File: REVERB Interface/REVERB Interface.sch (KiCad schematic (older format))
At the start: 17 parts, among them J1 RPiZeroW, J2 Iridium, J3 APRS, J4 Antenna, J5 MAX3232BOB, J5 USB, J6 USBSER2, J7 USBSER3, J8 USBSER1, U1 AT25P, U2 MAX3232

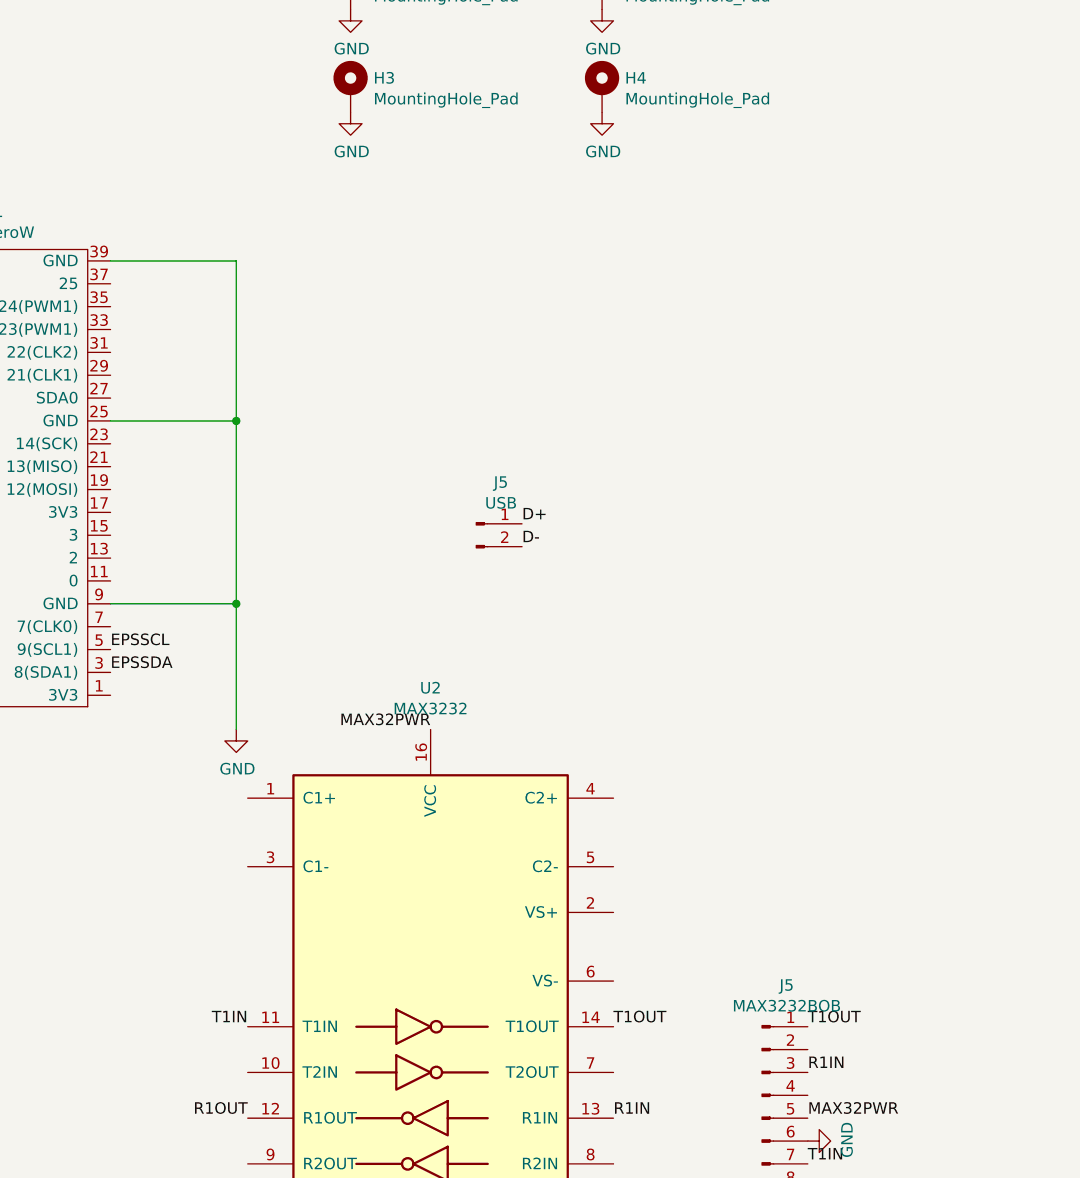
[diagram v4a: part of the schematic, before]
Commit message: add capacitors to max3232
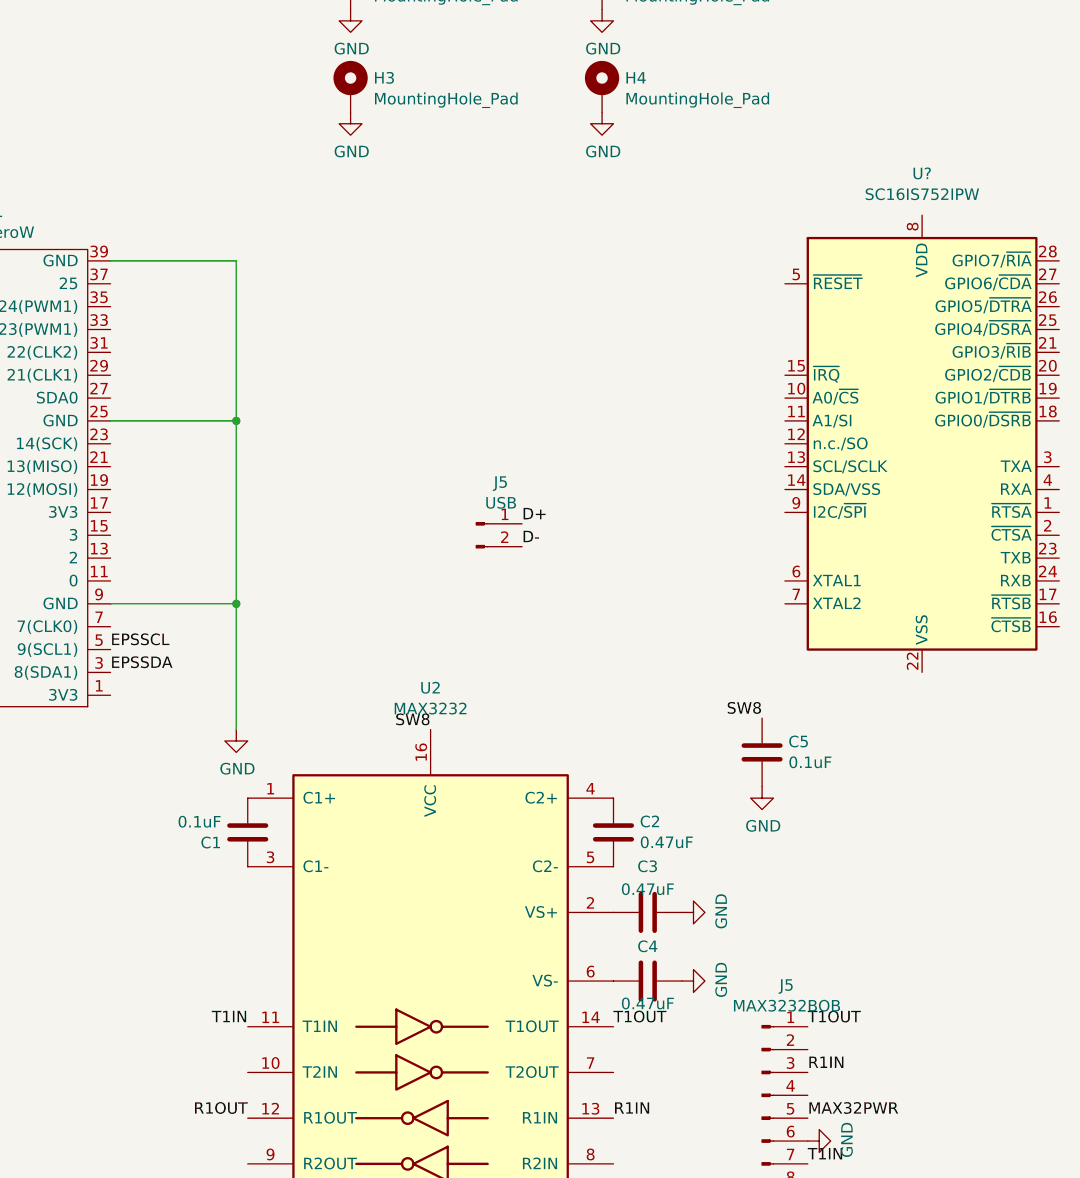
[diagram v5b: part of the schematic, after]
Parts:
- added C1, C5: 0.1uF, symbol Device:C
- added C2, C3, C4: 0.47uF, symbol Device:C
- added U?: SC16IS752IPW, Package_SO:TSSOP-28_4.4x9.7mm_P0.65mm, symbol Interface_UART:SC16IS752IPW
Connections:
- net GND: now also C3.1, C4.1, C5.2
- net MAX32PWR: no longer U2.16 (VCC)
- net SW8: now also U2.16 (VCC), C5.1
- net at U2.1 (C1+): now also C1.2
- net at U2.2 (VS+): now also C3.2
- net at U2.3 (C1-): now also C1.1
- net at U2.4 (C2+): now also C2.1
- net at U2.5 (C2-): now also C2.2
- net at U2.6 (VS-): now also C4.2
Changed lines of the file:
@@
 $EndComp
 Text Label 8800 4000 2    50   ~ 0
-MAX32PWR
+SW8
 Text Label 10450 5900 0    50   ~ 0
 T1IN
@@
 	0    1    1    0
 $EndComp
+$Comp
+L Device:C C1
+U 1 1 615D0719
+P 8000 4450
+F 0 "C1" H 8115 4496 50  0000 L CNN
+F 1 "0.1uF" H 8115 4405 50  0000 L CNN
+F 2 "" H 8038 4300 50  0001 C CNN
+F 3 "~" H 8000 4450 50  0001 C CNN
+	1    8000 4450
+	-1   0    0    1
+$EndComp
+$Comp
+L Device:C C2
+U 1 1 615D158A
+P 9600 4450
+F 0 "C2" H 9715 4496 50  0000 L CNN
+F 1 "0.47uF" H 9715 4405 50  0000 L CNN
+F 2 "" H 9638 4300 50  0001 C CNN
+F 3 "~" H 9600 4450 50  0001 C CNN
+	1    9600 4450
+	1    0    0    -1
+$EndComp
+$Comp
+L Device:C C3
+U 1 1 615D2368
+P 9750 4800
+F 0 "C3" V 9550 4800 50  0000 C CNN
+F 1 "0.47uF" V 9650 4800 50  0000 C CNN
+F 2 "" H 9788 4650 50  0001 C CNN
+F 3 "~" H 9750 4800 50  0001 C CNN
+	1    9750 4800
+	0    1    1    0
+$EndComp
+$Comp
+L Device:C C4
+U 1 1 615D50CA
+P 9750 5100
+F 0 "C4" V 9600 5100 50  0000 C CNN
+F 1 "0.47uF" V 9850 5100 50  0000 C CNN
+F 2 "" H 9788 4950 50  0001 C CNN
+F 3 "~" H 9750 5100 50  0001 C CNN
+	1    9750 5100
+	0    1    1    0
+$EndComp
+$Comp
+L power:GND #PWR?
+U 1 1 615D6BCC
+P 9900 5100
+F 0 "#PWR?" H 9900 4850 50  0001 C CNN
+F 1 "GND" H 9905 4927 50  0000 C CNN
+F 2 "" H 9900 5100 50  0001 C CNN
+F 3 "" H 9900 5100 50  0001 C CNN
+	1    9900 5100
+	0    -1   -1   0
+$EndComp
+$Comp
+L power:GND #PWR?
+U 1 1 615D7B6F
+P 9900 4800
+F 0 "#PWR?" H 9900 4550 50  0001 C CNN
+F 1 "GND" H 9905 4627 50  0000 C CNN
+F 2 "" H 9900 4800 50  0001 C CNN
+F 3 "" H 9900 4800 50  0001 C CNN
+	1    9900 4800
+	0    -1   -1   0
+$EndComp
+$Comp
+L Device:C C5
+U 1 1 615D8C42
+P 10250 4100
+F 0 "C5" H 10365 4146 50  0000 L CNN
+F 1 "0.1uF" H 10365 4055 50  0000 L CNN
+F 2 "" H 10288 3950 50  0001 C CNN
+F 3 "~" H 10250 4100 50  0001 C CNN
+	1    10250 4100
+	1    0    0    -1
+$EndComp
+Text Label 10250 3950 2    50   ~ 0
+SW8
+$Comp
+L power:GND #PWR?
+U 1 1 615DB22D
+P 10250 4250
+F 0 "#PWR?" H 10250 4000 50  0001 C CNN
+F 1 "GND" H 10255 4077 50  0000 C CNN
+F 2 "" H 10250 4250 50  0001 C CNN
+F 3 "" H 10250 4250 50  0001 C CNN
+	1    10250 4250
+	1    0    0    -1
+$EndComp
+$Comp
+L Interface_UART:SC16IS752IPW U?
+U 1 1 615DC7E1
+P 10950 2750
+F 0 "U?" H 10950 3931 50  0000 C CNN
+F 1 "SC16IS752IPW" H 10950 3840 50  0000 C CNN
+F 2 "Package_SO:TSSOP-28_4.4x9.7mm_P0.65mm" H 10950 1200 50  0001 C CNN
+F 3 "https://www.nxp.com/docs/en/data-sheet/SC16IS752_SC16IS762.pdf" H 10950 1350 50  0001 C CNN
+	1    10950 2750
+	1    0    0    -1
+$EndComp
 $EndSCHEMATC

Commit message: wiring work
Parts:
- added J8: USB, symbol Connector:Conn_01x02_Male
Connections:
- net D+: now also J8.1 (Pin_1)
- net D-: now also J8.2 (Pin_2)
- net EPSSCL: now also J4.7 (Pin_7), J4.8 (Pin_8)
- net EPSSDA: now also J4.2 (Pin_2), J4.4 (Pin_4)
- net GND: now also J3.16 (Pin_16), J4.3 (Pin_3), J4.5 (Pin_5), J4.9 (Pin_9), J6.9 (Pin_9)
- net SW4: now also J3.18 (Pin_18)
- net SW6: now also J4.1 (Pin_1), J4.6 (Pin_6)
- net SW7: now also J6.12 (Pin_12)
- net APRSRX: now reaches J3.4 (Pin_4)
- net APRSRX: now also J6.7 (Pin_7)
- net APRSTX: now reaches J3.6 (Pin_6)
- net APRSTX: now also J6.8 (Pin_8)
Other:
- moved on the sheet: J7
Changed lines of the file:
@@
 L Connector:Conn_01x06_Male J7
 U 1 1 615DBA1F
-P 4800 6400
-F 0 "J7" V 4862 6644 50  0000 L CNN
-F 1 "USBSER3" V 4953 6644 50  0000 L CNN
-F 2 "" H 4800 6400 50  0001 C CNN
-F 3 "~" H 4800 6400 50  0001 C CNN
-	1    4800 6400
-	0    1    1    0
+P 4650 4700
+F 0 "J7" V 4712 4944 50  0000 L CNN
+F 1 "USBSER3" V 4803 4944 50  0000 L CNN
+F 2 "" H 4650 4700 50  0001 C CNN
+F 3 "~" H 4650 4700 50  0001 C CNN
+	1    4650 4700
+	0    -1   -1   0
 $EndComp
 $Comp
@@
 	1    0    0    -1
 $EndComp
+$Comp
+L Connector:Conn_01x02_Male J8
+U 1 1 615E4914
+P 4750 6150
+F 0 "J8" H 4858 6331 50  0000 C CNN
+F 1 "USB" H 4858 6240 50  0000 C CNN
+F 2 "" H 4750 6150 50  0001 C CNN
+F 3 "~" H 4750 6150 50  0001 C CNN
+	1    4750 6150
+	0    1    1    0
+$EndComp
+Text Label 4750 6350 3    50   ~ 0
+D+
+Text Label 4650 6350 3    50   ~ 0
+D-
+Text Label 5100 6150 0    50   ~ 0
+SW7
+$Comp
+L power:GND #PWR?
+U 1 1 615E7235
+P 5100 5850
+F 0 "#PWR?" H 5100 5600 50  0001 C CNN
+F 1 "GND" H 5105 5677 50  0000 C CNN
+F 2 "" H 5100 5850 50  0001 C CNN
+F 3 "" H 5100 5850 50  0001 C CNN
+	1    5100 5850
+	0    -1   -1   0
+$EndComp
+Text Label 5100 5750 0    50   ~ 0
+APRSTX
+Text Label 5100 5650 0    50   ~ 0
+APRSRX
+Text Label 1150 5000 0    50   ~ 0
+SW6
+Text Label 1150 5500 0    50   ~ 0
+SW6
+Text Label 1150 5650 0    50   ~ 0
+EPSSCL
+Text Label 1300 5300 0    50   ~ 0
+EPSSDA
+Wire Wire Line
+	1150 5700 1150 5600
+Wire Wire Line
+	1150 5300 1300 5300
+Wire Wire Line
+	1300 5300 1300 5100
+Wire Wire Line
+	1300 5100 1150 5100
+Wire Wire Line
+	1150 5200 850  5200
+Wire Wire Line
+	850  5200 850  5400
+Wire Wire Line
+	850  5400 1150 5400
+Wire Wire Line
+	1150 5800 850  5800
+Wire Wire Line
+	850  5800 850  5400
+Connection ~ 850  5400
+Wire Wire Line
+	850  5800 850  5900
+Connection ~ 850  5800
+$Comp
+L power:GND #PWR?
+U 1 1 615ED1B0
+P 850 5900
+F 0 "#PWR?" H 850 5650 50  0001 C CNN
+F 1 "GND" H 855 5727 50  0000 C CNN
+F 2 "" H 850 5900 50  0001 C CNN
+F 3 "" H 850 5900 50  0001 C CNN
+	1    850  5900
+	1    0    0    -1
+$EndComp
+Text Label 2600 5850 0    50   ~ 0
+SW4
+Wire Wire Line
+	2600 5750 2850 5750
+Wire Wire Line
+	2850 5750 2850 5850
+$Comp
+L power:GND #PWR?
+U 1 1 615F0738
+P 2850 5850
+F 0 "#PWR?" H 2850 5600 50  0001 C CNN
+F 1 "GND" H 2855 5677 50  0000 C CNN
+F 2 "" H 2850 5850 50  0001 C CNN
+F 3 "" H 2850 5850 50  0001 C CNN
+	1    2850 5850
+	1    0    0    -1
+$EndComp
+Text Label 2600 5250 0    50   ~ 0
+APRSTX
+Text Label 2600 5150 0    50   ~ 0
+APRSRX
 $EndSCHEMATC

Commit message: footprint associations
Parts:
- C1, C2, C3, C4, C5: footprint (none) -> Capacitor_SMD:C_0805_2012Metric_Pad1.18x1.45mm_HandSolder
- H1, H2: footprint (none) -> Connector_PinSocket_2.54mm:PinSocket_2x26_P2.54mm_Vertical
- J1: footprint (none) -> Connector_PinSocket_2.54mm:PinSocket_2x20_P2.54mm_Vertical
- J10: renamed from J5; footprint (none) -> Connector_PinSocket_2.54mm:PinSocket_1x02_P2.54mm_Vertical
- J2: footprint (none) -> Connector_PinSocket_2.54mm:PinSocket_2x08_P2.54mm_Vertical
- J3: footprint (none) -> Connector_PinSocket_2.54mm:PinSocket_2x10_P2.54mm_Vertical
- J5: footprint (none) -> Connector_PinSocket_2.54mm:PinSocket_1x10_P2.54mm_Vertical
- J6, J8: footprint (none) -> Connector_PinSocket_2.54mm:PinSocket_1x12_P2.54mm_Vertical
- J7: footprint (none) -> Connector_PinSocket_2.54mm:PinSocket_1x06_P2.54mm_Vertical
- J9: renamed from J8; footprint (none) -> Connector_PinSocket_2.54mm:PinSocket_1x02_P2.54mm_Vertical
- M1: renamed from H1; footprint (none) -> MountingHole:MountingHole_3.2mm_M3_DIN965_Pad_TopBottom
- M2: renamed from H2; footprint (none) -> MountingHole:MountingHole_3.2mm_M3_DIN965_Pad_TopBottom
- M3: renamed from H3; footprint (none) -> MountingHole:MountingHole_3.2mm_M3_DIN965_Pad_TopBottom
- M4: renamed from H4; footprint (none) -> MountingHole:MountingHole_3.2mm_M3_DIN965_Pad_TopBottom
- gave numbers to parts that had none: 1
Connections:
- net GND: now also J2.5 (Pin_5)
- net R1IN: now also J2.13 (Pin_13)
- net SW3: now also J2.3 (Pin_3)
- net T1OUT: now also J2.11 (Pin_11)
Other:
- moved on the sheet: J2

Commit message: create board, finish footprint association
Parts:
- removed U1: AT25P, symbol Memory_EEPROM:AT25xxx
- H1, H2: footprint Connector_PinSocket_2.54mm:PinSocket_2x26_P2.54mm_Vertical -> REVERB Interface:PinSocket_2x26_P2.54mm_Vertical
- J4: footprint (none) -> REVERB Interface:1.25mmPitchHeader
- U2: footprint (none) -> REVERB Interface:Texas_Instruments-MAX3232ID
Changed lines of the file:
@@
 F 0 "H2" V 2996 2979 50  0000 L CNN
 F 1 "EPS Stack Header 1" V 2905 2979 50  0000 L CNN
-F 2 "Connector_PinSocket_2.54mm:PinSocket_2x26_P2.54mm_Vertical" H 2900 1700 50  0001 C CNN
+F 2 "REVERB Interface:PinSocket_2x26_P2.54mm_Vertical" H 2900 1700 50  0001 C CNN
 F 3 "~" H 2900 1700 50  0001 C CNN
 	1    2900 1700
@@
 F 0 "H1" V 2996 4629 50  0000 L CNN
 F 1 "EPS Stack Header 2" V 2905 4629 50  0000 L CNN
-F 2 "Connector_PinSocket_2.54mm:PinSocket_2x26_P2.54mm_Vertical" H 2900 3350 50  0001 C CNN
+F 2 "REVERB Interface:PinSocket_2x26_P2.54mm_Vertical" H 2900 3350 50  0001 C CNN
 F 3 "~" H 2900 3350 50  0001 C CNN
 	1    2900 3350
@@
 $EndComp
 $Comp
-L Memory_EEPROM:AT25xxx U1
-U 1 1 615C353F
-P 6200 5650
-F 0 "U1" H 6200 6131 50  0000 C CNN
-F 1 "AT25P" H 6200 6040 50  0000 C CNN
-F 2 "" H 6200 5650 50  0001 C CNN
-F 3 "http://ww1.microchip.com/downloads/en/DeviceDoc/Atmel-8707-SEEPROM-AT25010B-020B-040B-Datasheet.pdf" H 6200 5650 50  0001 C CNN
-	1    6200 5650
-	1    0    0    -1
-$EndComp
-$Comp
 L Connector:Conn_01x09_Male J4
 U 1 1 615C48DD
@@
 F 0 "J4" H 1058 5981 50  0000 C CNN
 F 1 "Antenna" H 1058 5890 50  0000 C CNN
-F 2 "" H 950 5400 50  0001 C CNN
+F 2 "REVERB Interface:1.25mmPitchHeader" H 950 5400 50  0001 C CNN
 F 3 "~" H 950 5400 50  0001 C CNN
 	1    950  5400
@@
 F 0 "U2" H 8800 6581 50  0000 C CNN
 F 1 "MAX3232" H 8800 6490 50  0000 C CNN
-F 2 "" H 8850 4150 50  0001 L CNN
+F 2 "REVERB Interface:Texas_Instruments-MAX3232ID" H 8850 4150 50  0001 L CNN
 F 3 "https://datasheets.maximintegrated.com/en/ds/MAX3222-MAX3241.pdf" H 8800 5300 50  0001 C CNN
 	1    8800 5200
